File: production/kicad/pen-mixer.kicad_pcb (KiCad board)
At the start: 4 copper layers, 12.9 x 34.9 mm, 32 parts, among them J1 USB-C 16P, J2 BAT, SW1 EVQP7C01P, U1 ISP1807-LR, U2 LSM6DS3TR-C, U3 MCP73831T-2ACI/OT, U4 TPS7A0533PDBV

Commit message: free nfc pins from imu
Disconnect IMU_INT1/INT2 from U1 P0.09/P0.10 (NFC1/NFC2) so the NFC
antenna can use them; the firmware polls the IMU and never used the
interrupts. Schematic: 4 wires and 4 labels removed, no-connect flags on
U1 pins 2, 4 and U2 INT1, INT2. PCB: 24 tracks and vias and 4 pad nets
removed. DRC 0 violations, 0 unconnected; ERC unchanged; netlist matches
reference-nets.json after the four intended removals.

Claude-Session: https://claude.ai/code/session_01Q1V828NK1ouT6YXKEbiFUx
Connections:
- U1 pad 2: IMU_INT1 -> (no net)
- U1 pad 4: IMU_INT2 -> (no net)
- U2 pad 4: IMU_INT1 -> (no net)
- U2 pad 9: IMU_INT2 -> (no net)
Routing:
- net IMU_INT2: track 15.4 -> 0.00 mm, vias 2 -> 0
- net IMU_INT1: track 15.2 -> 0.00 mm, vias 2 -> 0
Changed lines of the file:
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@@
 			(layers "F.Cu" "F.Mask" "F.Paste")
 			(roundrect_rratio 0.25)
-			(net "IMU_INT1")
 		)
 		(pad "5" smd roundrect
@@
 			(layers "F.Cu" "F.Mask" "F.Paste")
 			(roundrect_rratio 0.25)
-			(net "IMU_INT2")
 		)
 		(pad "10" smd roundrect
@@
 			(size 0.4 0.4)
 			(layers "F.Cu" "F.Mask" "F.Paste")
-			(net "IMU_INT1")
 		)
 		(pad "3" smd rect
@@
 			(size 0.4 0.4)
 			(layers "F.Cu" "F.Mask" "F.Paste")
-			(net "IMU_INT2")
 		)
 		(pad "5" smd rect
@@
 	)
 	(segment
-		(start 106.2619 53.4519)
-		(end 106.2619 54.676)
-		(width 0.15)
-		(layer "F.Cu")
-		(net "IMU_INT1")
-	)
-	(segment
-		(start 97.1829 58.7257)
-		(end 97.6732 58.7257)
-		(width 0.1124)
-		(layer "F.Cu")
-		(net "IMU_INT1")
-	)
-	(segment
-		(start 97.6732 58.7257)
-		(end 97.8327 58.8852)
-		(width 0.1124)
-		(layer "F.Cu")
-		(net "IMU_INT1")
-	)
-	(segment
-		(start 105.8952 53.0852)
-		(end 106.2619 53.4519)
-		(width 0.15)
-		(layer "F.Cu")
-		(net "IMU_INT1")
-	)
-	(via
-		(at 106.2619 54.676)
-		(size 0.45)
-		(drill 0.2)
-		(layers "F.Cu" "B.Cu")
-		(net "IMU_INT1")
-	)
-	(via
-		(at 97.1829 58.7257)
-		(size 0.45)
-		(drill 0.2)
-		(layers "F.Cu" "B.Cu")
-		(net "IMU_INT1")
-	)
-	(segment
-		(start 106.2619 54.676)
-		(end 105.5599 53.974)
-		(width 0.15)
-		(layer "In1.Cu")
-		(net "IMU_INT1")
-	)
-	(segment
-		(start 105.5599 53.974)
-		(end 99.4872 53.974)
-		(width 0.15)
-		(layer "In1.Cu")
-		(net "IMU_INT1")
-	)
-	(segment
-		(start 99.4872 53.974)
-		(end 97.1829 56.2783)
-		(width 0.15)
-		(layer "In1.Cu")
-		(net "IMU_INT1")
-	)
-	(segment
-		(start 97.1829 56.2783)
-		(end 97.1829 58.7257)
-		(width 0.15)
-		(layer "In1.Cu")
-		(net "IMU_INT1")
-	)
-	(segment
-		(start 106.698 53.238)
-		(end 106.698 54.1837)
-		(width 0.15)
-		(layer "F.Cu")
-		(net "IMU_INT2")
-	)
-	(segment
-		(start 105.8952 52.4352)
-		(end 106.698 53.238)
-		(width 0.15)
-		(layer "F.Cu")
-		(net "IMU_INT2")
-	)
-	(segment
-		(start 99.4536 58.3343)
-		(end 100.1068 58.3343)
-		(width 0.15)
-		(layer "F.Cu")
-		(net "IMU_INT2")
-	)
-	(segment
-		(start 100.1068 58.3343)
-		(end 100.1577 58.3852)
-		(width 0.15)
-		(layer "F.Cu")
-		(net "IMU_INT2")
-	)
-	(via
-		(at 99.4536 58.3343)
-		(size 0.45)
-		(drill 0.2)
-		(layers "F.Cu" "B.Cu")
-		(net "IMU_INT2")
-	)
-	(via
-		(at 106.698 54.1837)
-		(size 0.45)
-		(drill 0.2)
-		(layers "F.Cu" "B.Cu")
-		(net "IMU_INT2")
-	)
-	(segment
-		(start 99.4536 58.3343)
-		(end 99.2793 58.16)
-		(width 0.15)
-		(layer "In1.Cu")
-		(net "IMU_INT2")
-	)
-	(segment
-		(start 99.2793 58.16)
-		(end 99.2793 54.5238)
-		(width 0.15)
-		(layer "In1.Cu")
-		(net "IMU_INT2")
-	)
-	(segment
-		(start 99.5874 54.2157)
-		(end 104.1875 54.2157)
-		(width 0.15)
-		(layer "In1.Cu")
-		(net "IMU_INT2")
-	)
-	(segment
-		(start 104.1875 54.2157)
-		(end 105.0682 55.0964)
-		(width 0.15)
-		(layer "In1.Cu")
-		(net "IMU_INT2")
-	)
-	(segment
-		(start 99.2793 54.5238)
-		(end 99.5874 54.2157)
-		(width 0.15)
-		(layer "In1.Cu")
-		(net "IMU_INT2")
-	)
-	(segment
-		(start 105.0682 55.0964)
-		(end 106.4375 55.0964)
-		(width 0.15)
-		(layer "In1.Cu")
-		(net "IMU_INT2")
-	)
-	(segment
-		(start 106.698 54.8359)
-		(end 106.698 54.1837)
-		(width 0.15)
-		(layer "In1.Cu")
-		(net "IMU_INT2")
-	)
-	(segment
-		(start 106.4375 55.0964)
-		(end 106.698 54.8359)
-		(width 0.15)
-		(layer "In1.Cu")
-		(net "IMU_INT2")
-	)
-	(segment

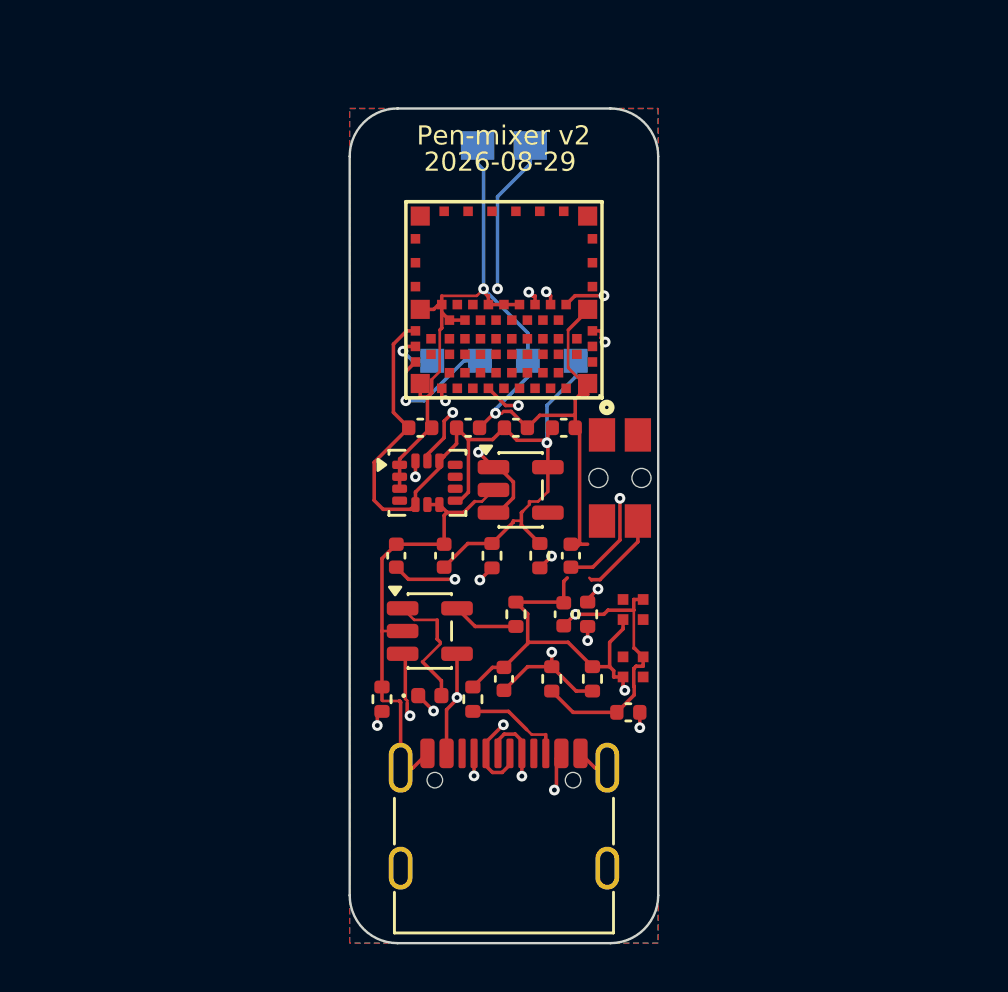
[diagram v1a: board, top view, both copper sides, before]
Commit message: add v3 star board
Regular five-point star, 40 mm tip to tip, antenna at the top prong with
its copper keep-out, all v2.1 parts kept. J1 becomes a vertical top-entry
USB-C (G-Switch GT-USB-7055E, C7450622, footprint and 3D model via
easyeda2kicad) so every prong stays identical; schematic netlist is
IDENTICAL to reference-nets.json. Routed with freerouting (0 unrouted),
GND pours on all four layers refilled, DRC 0 errors and 0 unconnected
with only the two accepted label text-thickness warnings, schematic
parity clean. U3 pad 2 connects solid to the pour (no room for two
thermal spokes). Renders in production/output/v3.

Claude-Session: https://claude.ai/code/session_01Q1V828NK1ouT6YXKEbiFUx
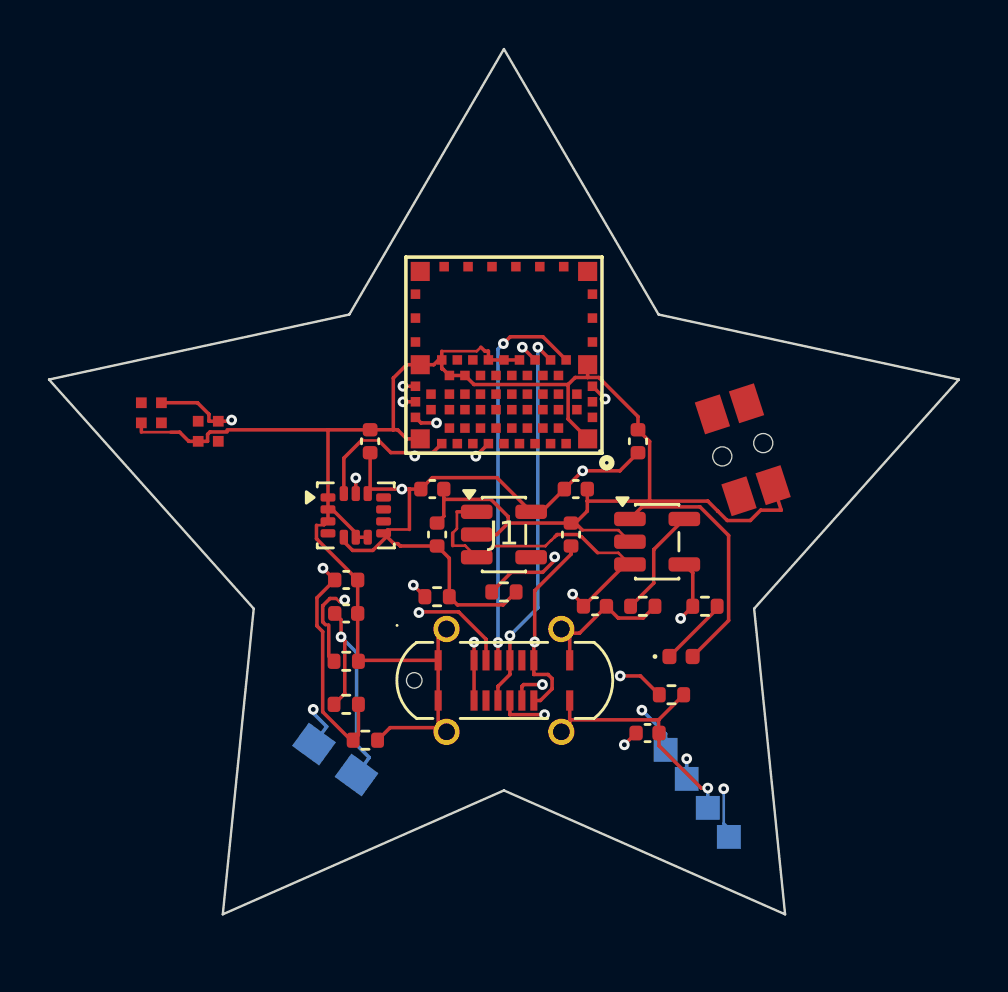
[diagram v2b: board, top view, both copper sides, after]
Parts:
- J1: value USB-C 16P -> USB-C 16P vertical; footprint USB_C_Receptacle_G-Switch_GT-USB-7010ASV -> pen-mixer:USB-C-SMD_GT-USB-7055E
- moved J2 26.6 mm to (95.1, 69.7), turned to 54 degrees
- moved LED2 22.8 mm to (87.5, 55.2)
- moved TP5 20.9 mm to (111.6, 72.9)
- moved TP4 20.2 mm to (110.7, 71.7)
- moved TP2 19.5 mm to (109.8, 70.5)
- moved LED1 19.3 mm to (89.8, 56.0)
- moved TP1 19.0 mm to (109.0, 69.3)
- moved D1 10.6 mm to (109.6, 65.4)
- moved U3 10.2 mm to (108.6, 60.6)
- moved R9 9.84 mm to (96.4, 68.9), turned to 0 degrees
- moved R8 8.66 mm to (95.6, 67.4), turned to 0 degrees
- moved R2 8.31 mm to (109.2, 67.0), turned to 0 degrees
- moved C10 7.78 mm to (95.6, 62.2), turned to 0 degrees
- moved J1 6.78 mm to (102.2, 66.4)
- moved R3 5.32 mm to (108.0, 63.3), turned to 0 degrees
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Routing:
- net SWDIO: track 2.02 -> 19.6 mm, vias 1 -> 2
- net SWDCLK: track 5.58 -> 20.7 mm, vias 1 -> 2
- net +3V3: track 36.0 -> 50.9 mm, vias 1 -> 4
- net GND: track 107.0 -> 119.1 mm, vias 4 -> 2
- net LED_A: track 12.1 -> 2.93 mm, vias 2 -> 0
- net USB_DM: track 23.2 -> 16.2 mm
- net CHG_STAT: track 5.51 -> 10.5 mm
- net CC1: track 6.53 -> 11.2 mm
- net VBAT: track 54.1 -> 58.5 mm, vias 5 -> 4
- net USB_DP: track 26.5 -> 22.3 mm, vias 2 -> 3
- net SCL: track 24.5 -> 21.1 mm
- net VBUS: track 40.8 -> 37.7 mm, vias 5 -> 4
- net CC2: track 4.24 -> 6.84 mm, vias 0 -> 2
- net IPROG: track 2.78 -> 4.58 mm
- net VBAT_SENSE: track 17.6 -> 19.1 mm
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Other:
- board size 12.9 x 34.9 mm -> 38 x 36.2 mm
- board text added: "2026-09-06"
- board text added: "Pen-mixer v3"
- board text removed: "2026-08-29"
- board text removed: "Pen-mixer v2"

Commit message: revise v3 star board
Flat side-entry USB-C recessed in the bottom notch, power button parallel
to the right arm's edge, LEDs mirrored left and right, test and battery
pads in lines parallel to the leg edges, passives aligned, rerouted with
freerouting (28 vias, was 34). Netlist identical to reference-nets.json;
DRC 0 errors, 0 unconnected.

Claude-Session: https://claude.ai/code/session_01FgTSApPZVavJw8HMjYxhL2
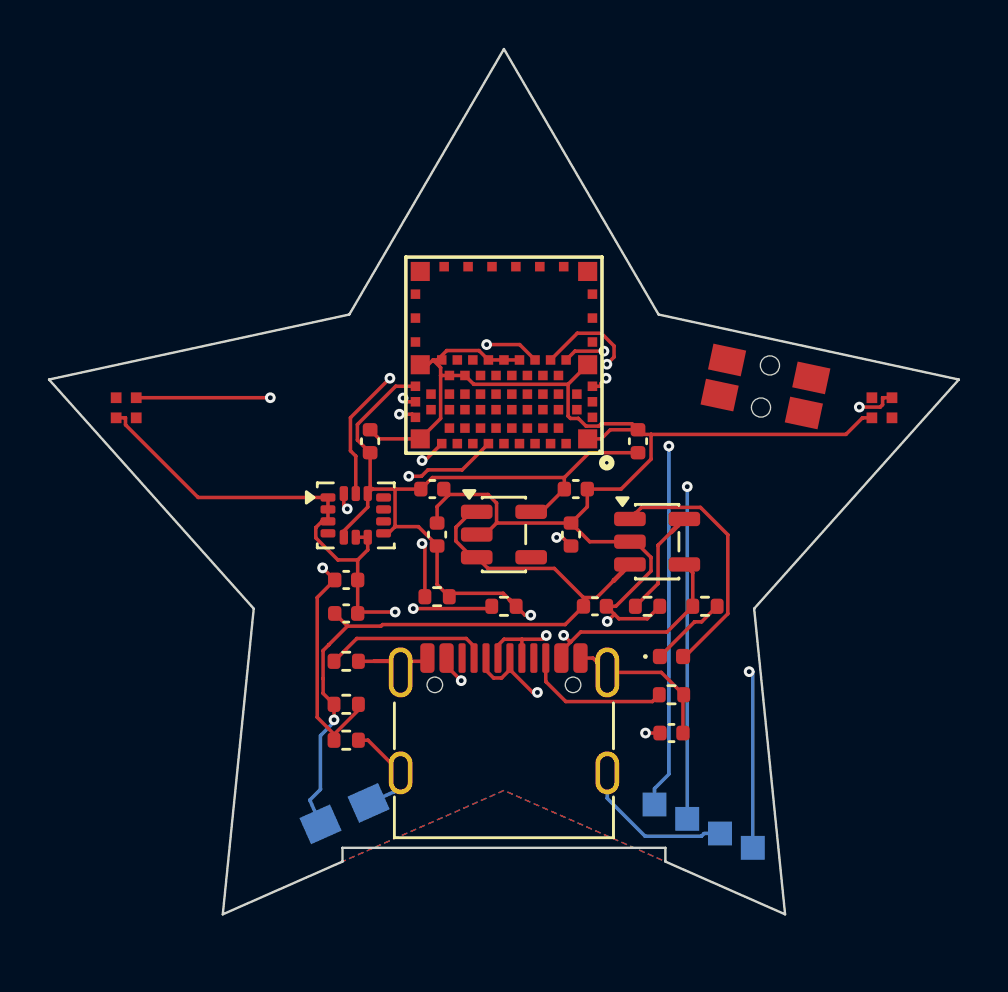
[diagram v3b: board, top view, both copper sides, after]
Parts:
- J1: value USB-C 16P vertical -> USB-C 16P; footprint pen-mixer:USB-C-SMD_GT-USB-7055E -> pen-mixer:GT-USB-7010ASV
- moved LED2 30.5 mm to (118.0, 55.0)
- moved LED1 3.57 mm to (86.4, 55.0)
- moved SW1 2.81 mm to (113.1, 54.1), turned to 168 degrees
- moved J1 2.79 mm to (102.2, 69.2)
- moved TP1 2.33 mm to (108.5, 71.6)
- moved J2 2.29 mm to (95.5, 72.0), turned to -66 degrees
- moved TP2 1.67 mm to (109.9, 72.2)
- moved TP4 1.19 mm to (111.2, 72.8)
- moved TP5 1.10 mm to (112.6, 73.4)
- moved C11 1.00 mm to (109.2, 68.6)
- moved R9 0.80 mm to (95.6, 68.9)
- moved R7 0.60 mm to (102.2, 63.3)
- moved D1 0.40 mm to (109.2, 65.4)
- moved R3 0.20 mm to (108.2, 63.3)
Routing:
- net VBAT: track 58.5 -> 93.6 mm
- net SCL: track 21.1 -> 29.6 mm
- net SWDIO: track 19.6 -> 27.8 mm
- net SWDCLK: track 20.7 -> 27.9 mm
- net GND: track 119.1 -> 126.0 mm
- net USB_DM: track 16.2 -> 23.0 mm
- net USB_DP: track 22.3 -> 18.1 mm, vias 3 -> 2
- net CC1: track 11.2 -> 7.25 mm, vias 2 -> 0
- net IPROG: track 4.58 -> 6.05 mm
- net SDA: track 12.5 -> 11.3 mm, vias 2 -> 3
- net VBUS: track 37.7 -> 36.9 mm
- net CHG_STAT: track 10.5 -> 11.0 mm
- net +3V3: track 50.9 -> 51.3 mm, vias 4 -> 2
- net CC2: track 6.84 -> 6.93 mm, vias 2 -> 0
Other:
- outline, holes or cut-outs redrawn
- board text added: "Pen-mixer v3.1"
- board text removed: "Pen-mixer v3"
